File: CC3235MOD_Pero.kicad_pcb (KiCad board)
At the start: 2 copper layers, 57.9 x 34.3 mm, 38 parts, among them J1 USB_B_Mini, J2 JTAG/SWD, SW1 Reset, SW2 SW_DIP_x03, SW3 User IO, U1 TLV1117-33, U2 CP2102N-A01-GQFN24, U3 CC3235MODSF12MOBR

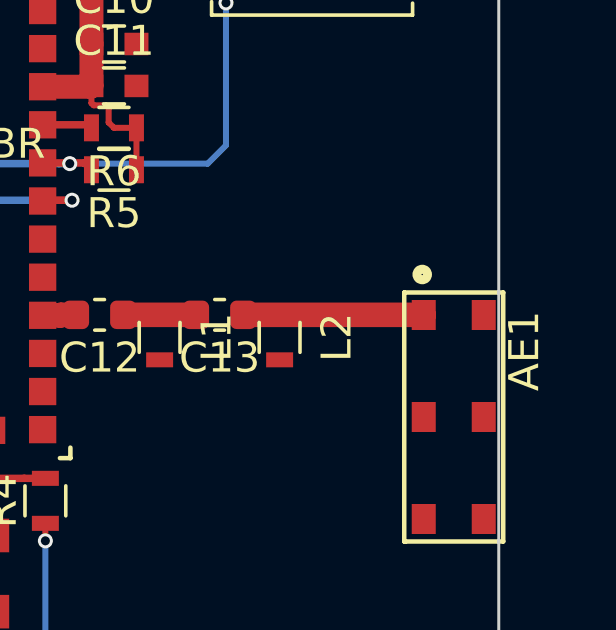
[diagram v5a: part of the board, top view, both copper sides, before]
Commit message: fixint antenna footprint
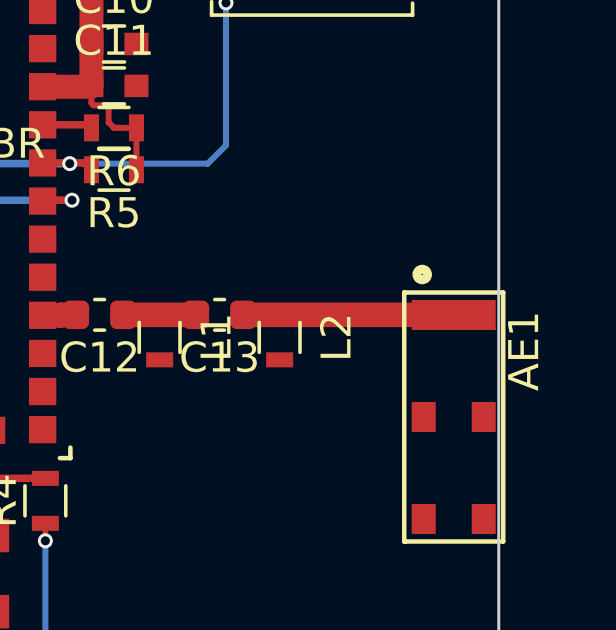
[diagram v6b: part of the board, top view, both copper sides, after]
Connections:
- AE1 pad 2: GND -> /ANTENNA
- J1 pad 4: Net-(J1-Pad4) -> (no net)
- J2 pad 7: Net-(J2-Pad7) -> (no net)
- U2 pad 1: Net-(U2-Pad1) -> (no net)
- U2 pad 10: Net-(U2-Pad10) -> (no net)
- U2 pad 11: Net-(U2-Pad11) -> (no net)
- U2 pad 12: Net-(U2-Pad12) -> (no net)
- U2 pad 13: Net-(U2-Pad13) -> (no net)
- U2 pad 14: Net-(U2-Pad14) -> (no net)
- U2 pad 15: Net-(U2-Pad15) -> (no net)
- U2 pad 16: Net-(U2-Pad16) -> (no net)
- U2 pad 17: Net-(U2-Pad17) -> (no net)
- U2 pad 18: Net-(U2-Pad18) -> (no net)
- U2 pad 19: Net-(U2-Pad19) -> (no net)
- U2 pad 22: Net-(U2-Pad22) -> (no net)
- U2 pad 23: Net-(U2-Pad23) -> (no net)
- U2 pad 24: Net-(U2-Pad24) -> (no net)
- U3 pad 10: Net-(U3-Pad10) -> (no net)
- U3 pad 11: Net-(U3-Pad11) -> (no net)
- U3 pad 13: Net-(U3-Pad13) -> (no net)
- U3 pad 14: Net-(U3-Pad14) -> (no net)
- U3 pad 15: Net-(U3-Pad15) -> (no net)
- U3 pad 17: Net-(U3-Pad17) -> (no net)
- U3 pad 19: Net-(U3-Pad19) -> (no net)
- U3 pad 20: Net-(U3-Pad20) -> (no net)
- U3 pad 33: Net-(U3-Pad33) -> (no net)
- U3 pad 39: Net-(U3-Pad39) -> (no net)
- U3 pad 4: Net-(U3-Pad4) -> (no net)
- U3 pad 41: Net-(U3-Pad41) -> (no net)
- U3 pad 42: Net-(U3-Pad42) -> (no net)
- U3 pad 44: Net-(U3-Pad44) -> (no net)
- U3 pad 45: Net-(U3-Pad45) -> (no net)
- U3 pad 48: Net-(U3-Pad48) -> (no net)
- U3 pad 49: Net-(U3-Pad49) -> (no net)
- U3 pad 5: Net-(U3-Pad5) -> (no net)
- U3 pad 50: Net-(U3-Pad50) -> (no net)
- U3 pad 51: Net-(U3-Pad51) -> (no net)
- U3 pad 52: Net-(U3-Pad52) -> (no net)
- U3 pad 53: Net-(U3-Pad53) -> (no net)
- U3 pad 54: Net-(U3-Pad54) -> (no net)
- U3 pad 6: Net-(U3-Pad6) -> (no net)
- U3 pad V: GND -> (no net)
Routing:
- net /ANTENNA: track 6.02 -> 7.77 mm
